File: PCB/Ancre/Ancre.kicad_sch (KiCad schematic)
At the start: 11 parts, among them IC1 TCAN1051VDRQ1, U1 OKI-78SR-5_1.5-W36-C, U2 DB301V-5.0-2P, U3 DB301V-5.0-2P

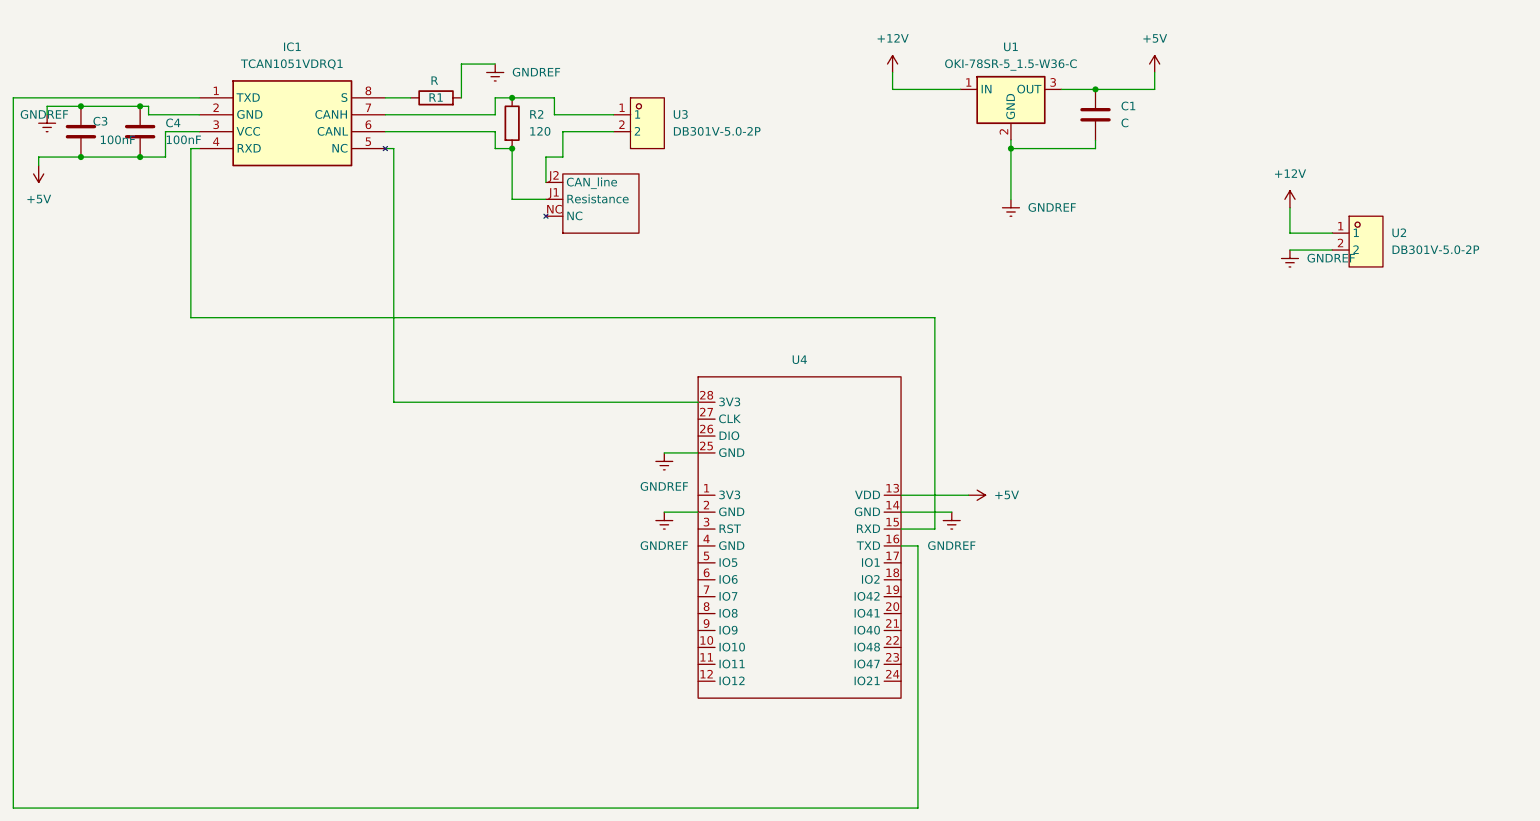
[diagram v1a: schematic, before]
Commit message: Ajout TCAN bornier bibliotheque
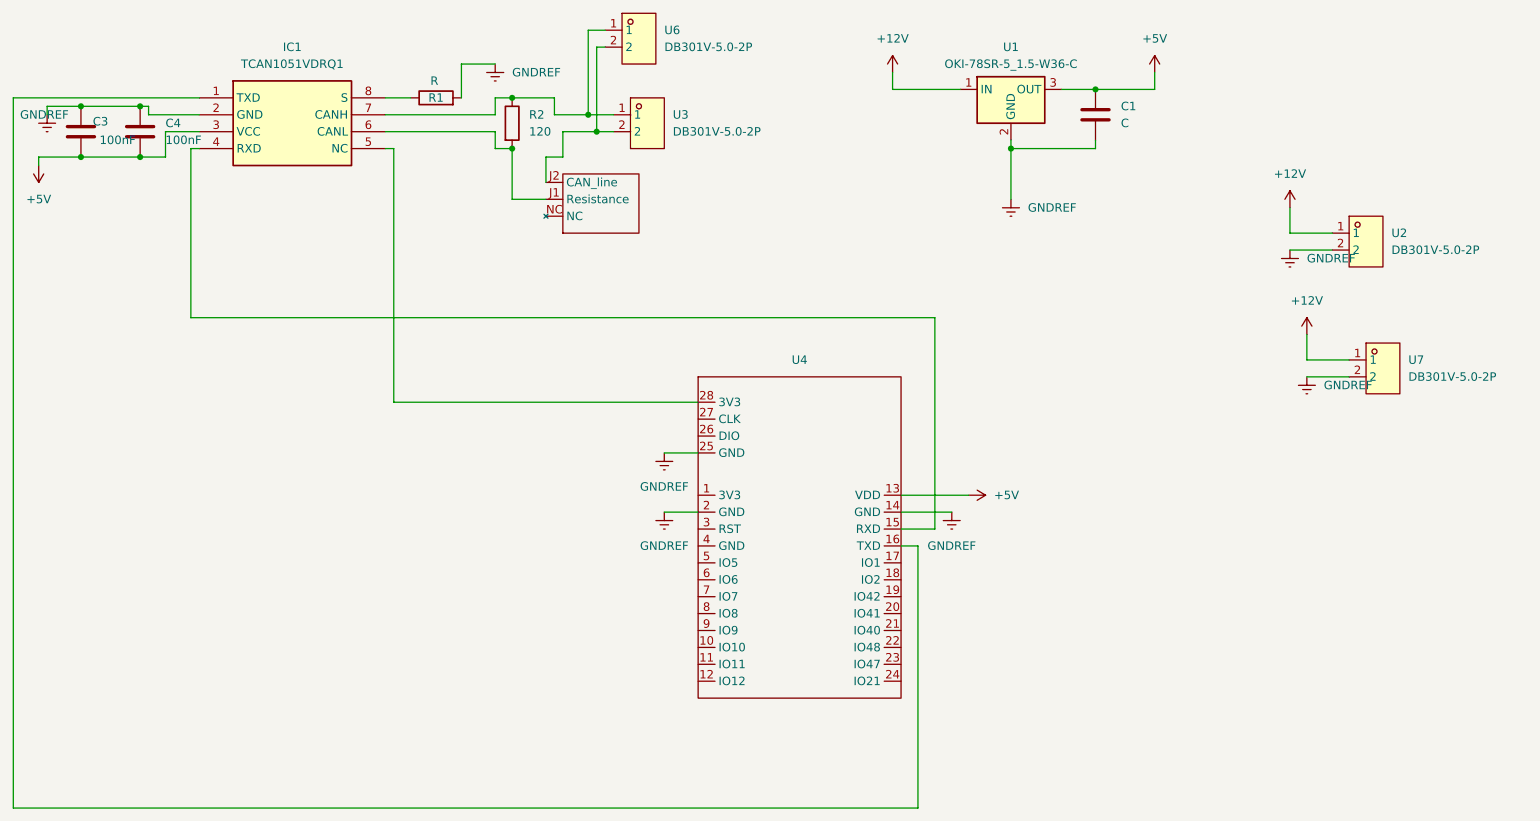
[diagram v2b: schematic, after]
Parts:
- added U6, U7: DB301V-5.0-2P, ancre2:CONN-TH_2P-P5.00_L7.6-W10.0 (1), symbol easyeda2kicad:DB301V-5.0-2P
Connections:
- net +12V: now also U7.1
- net GNDREF: now also U7.2
- net at IC1.7 (CANH), R2.1, U3.1: now also U6.1
- net at U3.2, U5.J2 (CAN_line): now also U6.2

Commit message: finalisation PCB ancre
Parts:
- U1: footprint Converter_DCDC:Converter_DCDC_Murata_OKI-78SR_Vertical -> Bibliotheque_Projet:Abaisseur 5v OKI; symbol Converter_DCDC:OKI-78SR-5_1.5-W36-C -> Bibliotheque_Projet:Abaisseur_OKI
- U6, U7: footprint ancre2:CONN-TH_2P-P5.00_L7.6-W10.0 (1) -> Bibliotheque_Projet:Bornier a vis; symbol easyeda2kicad:DB301V-5.0-2P -> Bibliotheque_Projet:Bornier_a_vis
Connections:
- net at IC1.7 (CANH), R2.1, U3.1: now also U6.2; no longer U6.1
- net at U3.2, U5.J2 (CAN_line): now also U6.1; no longer U6.2
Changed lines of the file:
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@@
+	(wire
+		(pts
+			(xy 134.62 45.72) (xy 134.62 55.88)
+		)
+		(stroke
+			(width 0)
+			(type default)
+		)
+	)
 	(wire
 		(pts
@@
 	(wire
 		(pts
+			(xy 135.89 43.18) (xy 137.16 43.18)
+		)
+		(stroke
+			(width 0)
+			(type default)
+		)
+	)
+	(wire
+		(pts
 			(xy 120.65 58.42) (xy 120.65 60.96)
 		)
@@
 	(wire
 		(pts
-			(xy 134.62 55.88) (xy 134.62 43.18)
-		)
-		(stroke
-			(width 0)
-			(type default)
-		)
-	)
-	(wire
-		(pts
 			(xy 198.12 60.96) (xy 198.12 68.58)
 		)
@@
 	(wire
 		(pts
-			(xy 135.89 45.72) (xy 137.16 45.72)
-		)
-		(stroke
-			(width 0)
-			(type default)
-		)
-	)
-	(wire
-		(pts
 			(xy 74.93 86.36) (xy 186.69 86.36)
 		)
@@
 	(wire
 		(pts
-			(xy 134.62 43.18) (xy 137.16 43.18)
-		)
-		(stroke
-			(width 0)
-			(type default)
-		)
-	)
-	(wire
-		(pts
 			(xy 68.58 55.88) (xy 68.58 54.61)
 		)
@@
 	(wire
 		(pts
+			(xy 135.89 43.18) (xy 135.89 58.42)
+		)
+		(stroke
+			(width 0)
+			(type default)
+		)
+	)
+	(wire
+		(pts
 			(xy 130.81 58.42) (xy 135.89 58.42)
 		)
@@
 	(wire
 		(pts
+			(xy 134.62 45.72) (xy 137.16 45.72)
+		)
+		(stroke
+			(width 0)
+			(type default)
+		)
+	)
+	(wire
+		(pts
 			(xy 186.69 86.36) (xy 186.69 118.11)
 		)
@@
 		(pts
 			(xy 210.82 52.07) (xy 219.71 52.07)
-		)
-		(stroke
-			(width 0)
-			(type default)
-		)
-	)
-	(wire
-		(pts
-			(xy 135.89 58.42) (xy 135.89 45.72)
 		)
 		(stroke
@@
 	)
 	(symbol
-		(lib_id "easyeda2kicad:DB301V-5.0-2P")
+		(lib_id "Bibliotheque_Projet:Bornier_a_vis")
 		(at 252.73 93.98 0)
 		(unit 1)
@@
 			)
 		)
-		(property "Footprint" "ancre2:CONN-TH_2P-P5.00_L7.6-W10.0 (1)"
+		(property "Footprint" "Bibliotheque_Projet:Bornier a vis"
 			(at 252.73 102.87 0)
 			(hide yes)
@@
 	)
 	(symbol
-		(lib_id "easyeda2kicad:DB301V-5.0-2P")
+		(lib_id "Bibliotheque_Projet:Bornier_a_vis")
 		(at 140.97 44.45 0)
 		(unit 1)
@@
 			)
 		)
-		(property "Footprint" "ancre2:CONN-TH_2P-P5.00_L7.6-W10.0 (1)"
+		(property "Footprint" "Bibliotheque_Projet:Bornier a vis"
 			(at 140.97 53.34 0)
 			(hide yes)
@@
 	)
 	(symbol
-		(lib_id "Converter_DCDC:OKI-78SR-5_1.5-W36-C")
+		(lib_id "Bibliotheque_Projet:Abaisseur_OKI")
 		(at 198.12 52.07 0)
 		(unit 1)
@@
 			)
 		)
-		(property "Footprint" "Converter_DCDC:Converter_DCDC_Murata_OKI-78SR_Vertical"
+		(property "Footprint" "Bibliotheque_Projet:Abaisseur 5v OKI"
 			(at 199.39 58.42 0)
 			(hide yes)

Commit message: nouvelle ancre pas fini
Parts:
- added C5: 100nF, Capacitor_THT:C_Axial_L3.8mm_D2.6mm_P7.50mm_Horizontal, symbol Device:C
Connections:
- net GNDREF: now also C5.1
- net at U3.2, U6.1: now also IC1.6 (CANL), U5.J1 (Resistance); no longer U5.J2 (CAN_line)
- net at IC1.5 (NC), U4.28 (3V3): now also C5.2
- new net: R2.2, U5.J2 (CAN_line)
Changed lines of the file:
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@@
-	)
-	(junction
-		(at 123.19 60.96)
-		(diameter 0)
-		(color 0 0 0 0)
 	)
 	(junction
@@
 	)
 	(junction
+		(at 120.65 62.23)
+		(diameter 0)
+		(color 0 0 0 0)
+	)
+	(junction
+		(at 105.41 67.31)
+		(diameter 0)
+		(color 0 0 0 0)
+	)
+	(junction
 		(at 198.12 60.96)
 		(diameter 0)
@@
 	(wire
 		(pts
+			(xy 123.19 66.04) (xy 128.27 66.04)
+		)
+		(stroke
+			(width 0)
+			(type default)
+		)
+	)
+	(wire
+		(pts
 			(xy 120.65 55.88) (xy 120.65 53.34)
 		)
@@
 	(wire
 		(pts
-			(xy 120.65 60.96) (xy 123.19 60.96)
-		)
-		(stroke
-			(width 0)
-			(type default)
-		)
-	)
-	(wire
-		(pts
 			(xy 115.57 48.26) (xy 120.65 48.26)
 		)
@@
 	(wire
 		(pts
+			(xy 123.19 60.96) (xy 123.19 66.04)
+		)
+		(stroke
+			(width 0)
+			(type default)
+		)
+	)
+	(wire
+		(pts
+			(xy 105.41 67.31) (xy 105.41 99.06)
+		)
+		(stroke
+			(width 0)
+			(type default)
+		)
+	)
+	(wire
+		(pts
 			(xy 205.74 52.07) (xy 210.82 52.07)
 		)
@@
 	(wire
 		(pts
-			(xy 105.41 60.96) (xy 105.41 99.06)
+			(xy 105.41 60.96) (xy 105.41 67.31)
 		)
 		(stroke
@@
 	(wire
 		(pts
-			(xy 123.19 68.58) (xy 123.19 60.96)
-		)
-		(stroke
-			(width 0)
-			(type default)
-		)
-	)
-	(wire
-		(pts
 			(xy 219.71 49.53) (xy 219.71 52.07)
 		)
@@
 	(wire
 		(pts
-			(xy 120.65 58.42) (xy 120.65 60.96)
+			(xy 120.65 58.42) (xy 120.65 62.23)
 		)
 		(stroke
@@
 	(wire
 		(pts
+			(xy 120.65 62.23) (xy 120.65 68.58)
+		)
+		(stroke
+			(width 0)
+			(type default)
+		)
+	)
+	(wire
+		(pts
 			(xy 184.15 120.65) (xy 181.61 120.65)
 		)
@@
 	(wire
 		(pts
-			(xy 128.27 68.58) (xy 123.19 68.58)
-		)
-		(stroke
-			(width 0)
-			(type default)
-		)
-	)
-	(wire
-		(pts
 			(xy 181.61 115.57) (xy 189.23 115.57)
 		)
@@
 	(wire
 		(pts
+			(xy 120.65 68.58) (xy 128.27 68.58)
+		)
+		(stroke
+			(width 0)
+			(type default)
+		)
+	)
+	(wire
+		(pts
 			(xy 104.14 58.42) (xy 120.65 58.42)
 		)
@@
 	(wire
 		(pts
-			(xy 128.27 66.04) (xy 128.27 62.23)
+			(xy 120.65 62.23) (xy 130.81 62.23)
 		)
 		(stroke
@@
 	(wire
 		(pts
+			(xy 101.6 74.93) (xy 101.6 78.74)
+		)
+		(stroke
+			(width 0)
+			(type default)
+		)
+	)
+	(wire
+		(pts
+			(xy 101.6 67.31) (xy 105.41 67.31)
+		)
+		(stroke
+			(width 0)
+			(type default)
+		)
+	)
+	(wire
+		(pts
 			(xy 210.82 59.69) (xy 210.82 60.96)
 		)
@@
 		(pts
 			(xy 48.26 53.34) (xy 76.2 53.34)
-		)
-		(stroke
-			(width 0)
-			(type default)
-		)
-	)
-	(wire
-		(pts
-			(xy 128.27 62.23) (xy 130.81 62.23)
 		)
 		(stroke
@@
 					(unit 1)
 				)
+			)
+		)
+	)
+	(symbol
+		(lib_id "Device:C")
+		(at 101.6 71.12 180)
+		(unit 1)
+		(body_style 1)
+		(exclude_from_sim no)
+		(in_bom yes)
+		(on_board yes)
+		(in_pos_files yes)
+		(dnp no)
+		(property "Reference" "C5"
+			(at 91.694 69.088 0)
+			(show_name no)
+			(do_not_autoplace no)
+			(effects
+				(font
+					(size 1.27 1.27)
+				)
+				(justify right)
+			)
+		)
+		(property "Value" "100nF"
+			(at 91.694 71.628 0)
+			(show_name no)
+			(do_not_autoplace no)
+			(effects
+				(font
+					(size 1.27 1.27)
+				)
+				(justify right)
+			)
+		)
+		(property "Footprint" "Capacitor_THT:C_Axial_L3.8mm_D2.6mm_P7.50mm_Horizontal"
+			(at 100.6348 67.31 0)
+			(hide yes)
+			(show_name no)
+			(do_not_autoplace no)
+			(effects
+				(font
+					(size 1.27 1.27)
+				)
+			)
+		)
+		(property "Datasheet" ""
+			(at 101.6 71.12 0)
+			(hide yes)
+			(show_name no)
+			(do_not_autoplace no)
+			(effects
+				(font
+					(size 1.27 1.27)
+				)
+			)
+		)
+		(property "Description" "Unpolarized capacitor"
+			(at 101.6 71.12 0)
+			(hide yes)
+			(show_name no)
+			(do_not_autoplace no)
+			(effects
+				(font
+					(size 1.27 1.27)
+				)
+			)
+		)
+		(pin "2"
+		)
+		(pin "1"
+		)
+		(instances
+			(project "Ancre"
+				(path "/d2e8c312-f361-4e5e-b264-be30272b880a"
+					(reference "C5")
+					(unit 1)
+				)
+			)
+		)
+	)
+	(symbol
+		(lib_id "power:GNDREF")
+		(at 101.6 78.74 0)
+		(unit 1)
+		(body_style 1)
+		(exclude_from_sim no)
+		(in_bom yes)
+		(on_board yes)
+		(in_pos_files yes)
+		(dnp no)
+		(property "Reference" "#PWR06"
+			(at 101.6 85.09 0)
+			(hide yes)
+			(show_name no)
+			(do_not_autoplace no)
+			(effects
+				(font
+					(size 1.27 1.27)
+				)
+			)
+		)
+		(property "Value" "GNDREF"
+			(at 91.186 79.756 0)
+			(show_name no)
+			(do_not_autoplace no)
+			(effects
+				(font
+					(size 1.27 1.27)
+				)
+				(justify left)
+			)
+		)
+		(property "Footprint" ""
+			(at 101.6 78.74 0)
+			(hide yes)
+			(show_name no)
+			(do_not_autoplace no)
+			(effects
+				(font
+					(size 1.27 1.27)
+				)
+			)
+		)
+		(property "Datasheet" ""
+			(at 101.6 78.74 0)
+			(hide yes)
+			(show_name no)
+			(do_not_autoplace no)
+			(effects
+				(font
+					(size 1.27 1.27)
+				)
+			)
+		)
+		(property "Description" "Power symbol creates a global label with name \"GNDREF\" , reference supply ground"
+			(at 101.6 78.74 0)
+			(hide yes)
+			(show_name no)
+			(do_not_autoplace no)
+			(effects
+				(font
+					(size 1.27 1.27)
+				)
+			)
+		)
+		(pin "1"
+		)
+		(instances
+			(project "Ancre"
+				(path "/d2e8c312-f361-4e5e-b264-be30272b880a"
+					(reference "#PWR06")
+					(unit 1)
+				)

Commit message: ancre fini ?
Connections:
- net at IC1.6 (CANL), U3.2, U6.1: now also U5.J2 (CAN_line); no longer U5.J1 (Resistance)
- net at R2.2: now also U5.J1 (Resistance); no longer U5.J2 (CAN_line)
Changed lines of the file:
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@@
+	)
+	(junction
+		(at 125.73 62.23)
+		(diameter 0)
+		(color 0 0 0 0)
 	)
 	(junction
@@
 	)
 	(junction
-		(at 120.65 62.23)
-		(diameter 0)
-		(color 0 0 0 0)
-	)
-	(junction
 		(at 105.41 67.31)
 		(diameter 0)
@@
 	(wire
 		(pts
-			(xy 123.19 66.04) (xy 128.27 66.04)
-		)
-		(stroke
-			(width 0)
-			(type default)
-		)
-	)
-	(wire
-		(pts
 			(xy 120.65 55.88) (xy 120.65 53.34)
 		)
@@
 	(wire
 		(pts
-			(xy 123.19 60.96) (xy 123.19 66.04)
+			(xy 123.19 60.96) (xy 123.19 68.58)
 		)
 		(stroke
@@
 	(wire
 		(pts
-			(xy 120.65 62.23) (xy 120.65 68.58)
-		)
-		(stroke
-			(width 0)
-			(type default)
-		)
-	)
-	(wire
-		(pts
 			(xy 184.15 120.65) (xy 181.61 120.65)
 		)
@@
 	(wire
 		(pts
+			(xy 123.19 68.58) (xy 128.27 68.58)
+		)
+		(stroke
+			(width 0)
+			(type default)
+		)
+	)
+	(wire
+		(pts
 			(xy 104.14 53.34) (xy 107.95 53.34)
 		)
@@
 	(wire
 		(pts
-			(xy 120.65 68.58) (xy 128.27 68.58)
-		)
-		(stroke
-			(width 0)
-			(type default)
-		)
-	)
-	(wire
-		(pts
 			(xy 104.14 58.42) (xy 120.65 58.42)
 		)
@@
 	(wire
 		(pts
+			(xy 125.73 66.04) (xy 125.73 62.23)
+		)
+		(stroke
+			(width 0)
+			(type default)
+		)
+	)
+	(wire
+		(pts
 			(xy 181.61 113.03) (xy 191.77 113.03)
 		)
@@
 	(wire
 		(pts
-			(xy 120.65 62.23) (xy 130.81 62.23)
+			(xy 120.65 62.23) (xy 125.73 62.23)
 		)
 		(stroke
@@
 	(wire
 		(pts
+			(xy 128.27 66.04) (xy 125.73 66.04)
+		)
+		(stroke
+			(width 0)
+			(type default)
+		)
+	)
+	(wire
+		(pts
 			(xy 52.07 62.23) (xy 58.42 62.23)
 		)
@@
 		)
 		(stroke
+			(width 0)
+			(type default)
+		)
+	)
+	(wire
+		(pts
+			(xy 125.73 62.23) (xy 130.81 62.23)
+		)
+		(stroke

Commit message: Ancre_v12_fini
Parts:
- C1: value C -> 10uF
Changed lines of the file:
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@@
 			)
 		)
-		(property "Value" "C"
+		(property "Value" "10uF"
 			(at 214.63 57.1499 0)
 			(show_name no)

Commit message: Update Ancre.kicad_sch
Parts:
- R1: value R -> 4.7K
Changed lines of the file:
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@@
 			)
 		)
-		(property "Value" "R"
+		(property "Value" "4.7K"
 			(at 111.506 50.8 90)
 			(show_name no)
